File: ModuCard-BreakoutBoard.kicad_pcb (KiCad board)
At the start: 4 copper layers, 85 x 97.7 mm, 55 parts, among them J1 09031967921, J10 USB_C_Receptacle_USB2.0_16P, J11 Barrel_Jack_Switch, J3 Conn_01x16_Pin, J4 Conn_01x16_Pin, J5 Conn_01x16_Pin, J6 Barrel_Jack_Switch, J7 Conn_01x02_Pin, J8 Conn_01x02_Pin, J9 RJ45_LED_Shielded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

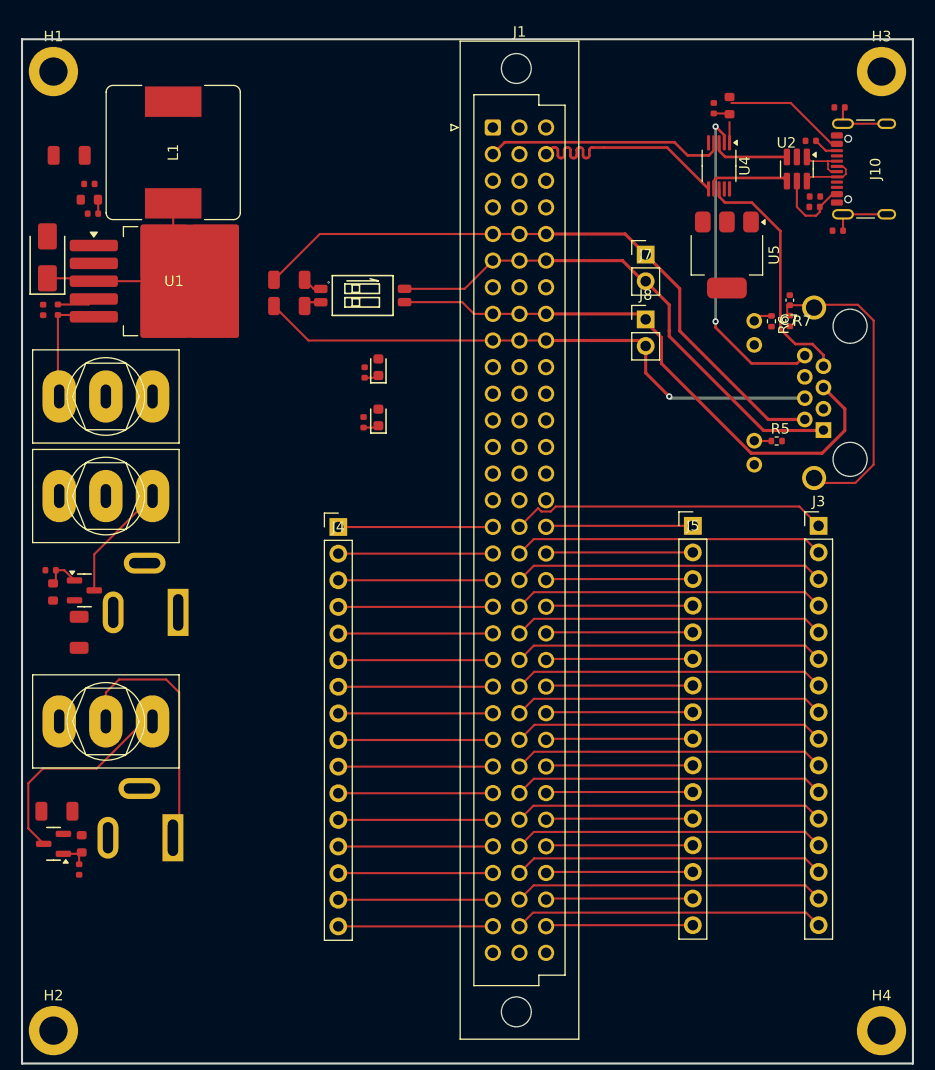
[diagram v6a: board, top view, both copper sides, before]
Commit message: Add mounting holes
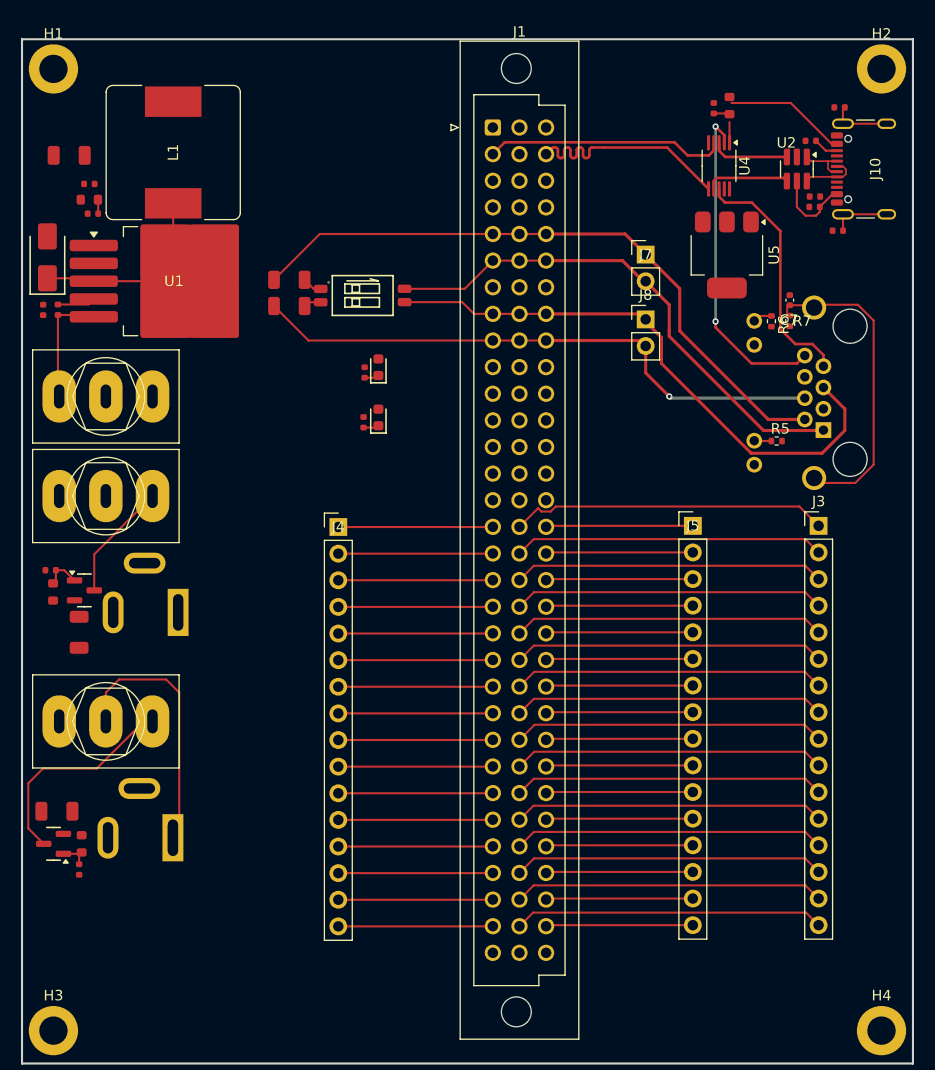
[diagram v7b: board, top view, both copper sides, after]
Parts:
- moved H2 121.1 mm to (172.0, 61.2)
- moved H3 120.9 mm to (93.0, 153.0)
- moved H1 0.25 mm to (93.0, 61.2)

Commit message: Change layout
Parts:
- removed C5: 100uF, PCM_JLCPCB:C_1206
- added C10: 470uF, PCM_JLCPCB:C_Plugin,D10xL16mm, F.Cu at (96.0, 68.5)
- S1: footprint PCM_JLCPCB:SW-SMD_218-2LPSTRF -> Button_Switch_THT:SW_DIP_SPSTx02_Slide_9.78x7.26mm_W7.62mm_P2.54mm
- moved C3 30.0 mm to (102.0, 112.5), turned to -90 degrees
- moved D5 20.7 mm to (123.5, 69.0)
- moved R4 20.7 mm to (122.2, 69.5)
- moved S1 3.46 mm to (119.2, 81.7), turned to 0 degrees
- moved R2 3.23 mm to (100.0, 75.1)
- moved C4 3.19 mm to (98.0, 75.0)
- moved L1 3.08 mm to (107.5, 69.2)
- moved R1 2.89 mm to (99.3, 73.7)
- moved U5 1.81 mm to (155.7, 79.9)
- moved D4 1.81 mm to (124.2, 96.3)
- moved R3 1.81 mm to (122.8, 96.8)
- moved C2 1.76 mm to (94.0, 114.0), turned to 0 degrees
- moved R11 0.73 mm to (92.0, 109.0)
- moved Q2 0.71 mm to (95.3, 110.9)
- moved U2 0.62 mm to (164.6, 70.8)
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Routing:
- net /Connector/CAN1.+: track 62.1 -> 0.00 mm
- net /Connector/CAN2.-: track 55.8 -> 0.00 mm, vias 1 -> 0
- net /Connector/CAN2.+: track 55.4 -> 0.00 mm
- net /Connector/CAN1.-: track 49.6 -> 0.00 mm
- net /RJ45/USB_RJ.+: track 31.3 -> 0.00 mm, vias 2 -> 0
- net Net-(C7-Pad1): track 30.4 -> 0.00 mm
- net /Connector/GPIOC0: track 30.4 -> 0.00 mm
- net /Connector/GPIOC8: track 29.7 -> 0.00 mm
- net /Connector/GPIOC6: track 29.7 -> 0.00 mm
- net /Connector/GPIOC9: track 29.7 -> 0.00 mm
- net /Connector/GPIOC13: track 29.7 -> 0.00 mm
- net /Connector/GPIOC4: track 29.6 -> 0.00 mm
- net /Connector/GPIOC3: track 29.6 -> 0.00 mm
- net /Connector/GPIOC12: track 29.6 -> 0.00 mm
- net /Connector/GPIOC7: track 29.6 -> 0.00 mm
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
